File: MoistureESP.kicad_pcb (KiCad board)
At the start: 2 copper layers, 106 parts, among them J1 Conn_01x02_Pin, J2 Conn_MoisturePCB, J3 Conn_DS18B20, J4 Conn_01x06_Pin, J5 Conn_01x03_Pin, J7 USB4110-GF-A, Q1 SSM6K513NU-LF, Q10 SI7137DP-T1-GE3, Q2 SSM6K513NU-LF, Q3 2N7002W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

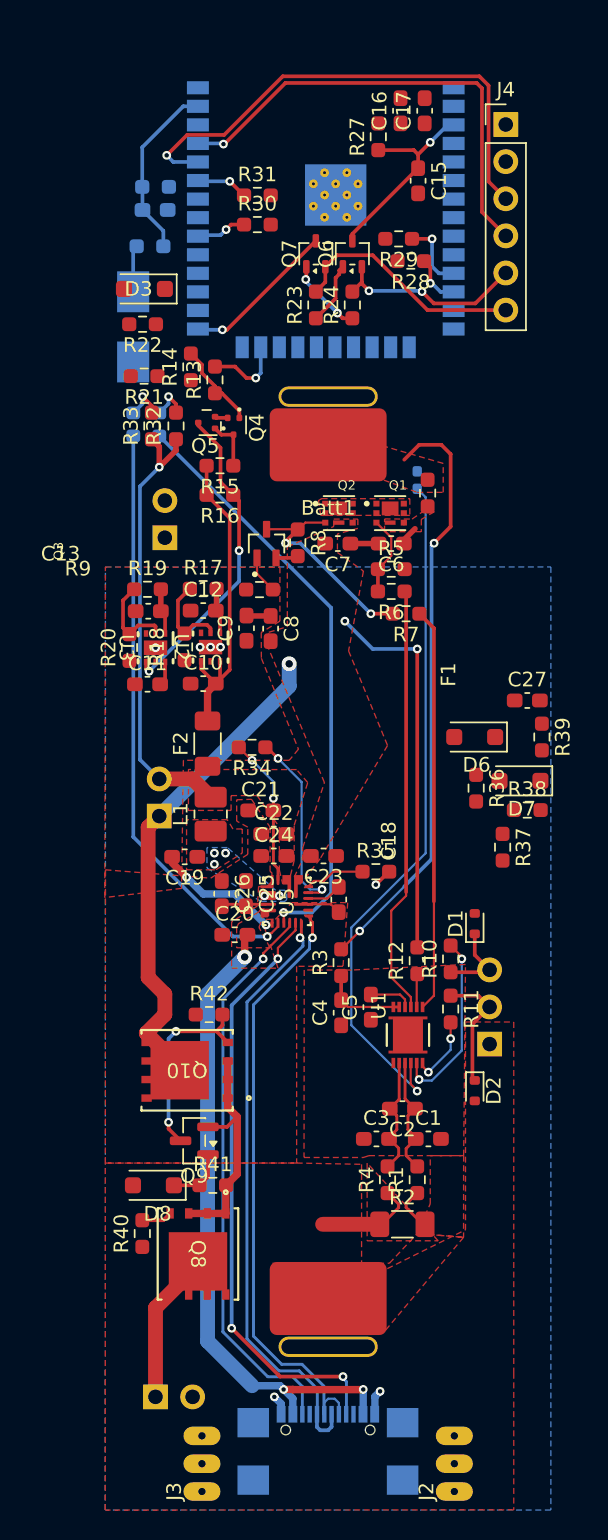
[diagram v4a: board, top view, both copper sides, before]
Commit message: Layout is finished with adding analog part, wiring the MCU ports and adding GNDD zones. Also add the nettie.
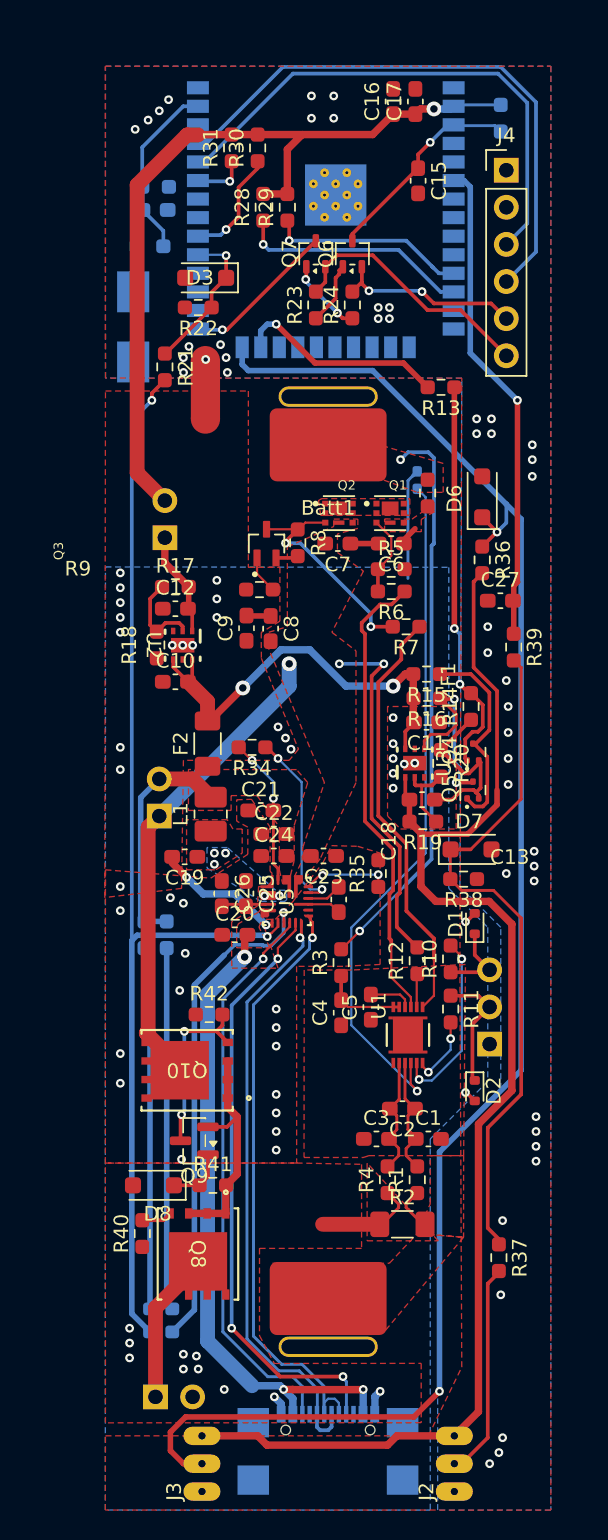
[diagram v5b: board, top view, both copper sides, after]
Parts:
- added NT1: NetTie_2, NetTie:NetTie-2_SMD_Pad2.0mm, F.Cu at (42.4, 75.7)
- R27, R32, R33: moved to B.Cu
- moved D5 61.3 mm to (38.6, 139.4)
- moved D4 61.3 mm to (40.1, 139.4)
- moved R32 34.8 mm to (39.8, 113.0), turned to -90 degrees
- moved R33 34.8 mm to (38.2, 113.0), turned to -90 degrees
- moved Q5 31.1 mm to (60.7, 103.1), turned to 90 degrees
- moved R14 30.1 mm to (60.6, 97.4)
- moved R37 28.1 mm to (62.5, 135.1)
- moved Q4 27.7 mm to (60.7, 100.5), turned to 90 degrees
- moved R19 24.6 mm to (57.3, 105.3), turned to 180 degrees
- moved C13 22.7 mm to (57.2, 103.8), turned to 180 degrees
- moved R20 22.7 mm to (58.5, 101.3), turned to -90 degrees
- moved R15 20.1 mm to (57.5, 95.2)
- moved R16 19.9 mm to (57.6, 96.8)
- moved U3 19.4 mm to (56.7, 101.3), turned to 90 degrees
- moved C11 19.3 mm to (57.5, 98.5), turned to 180 degrees
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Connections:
- D1 pad 2: GNDD -> GNDPWR
- D2 pad 2: GNDD -> GNDPWR
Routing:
- net /mcu/onewire_pin: track 0.00 -> 115.1 mm, vias 0 -> 2
- net Van: track 3.14 -> 93.6 mm
- net VDD: track 0.00 -> 55.7 mm, vias 0 -> 1
- net Net-(D7-K): track 0.00 -> 47.5 mm
- net /charger/~{INOK}: track 40.9 -> 77.5 mm, vias 1 -> 2
- net /mcu/analog_pin: track 0.00 -> 33.4 mm, vias 0 -> 1
- net Net-(D4-A): track 2.69 -> 24.8 mm, vias 1 -> 0
- net Net-(D5-A): track 2.74 -> 24.8 mm, vias 1 -> 0
- net Net-(Q4-G): track 6.06 -> 27.2 mm, vias 0 -> 2
- net GNDPWR: track 11.9 -> 31.8 mm, vias 7 -> 51
- net Vsys: track 31.0 -> 15.9 mm, vias 1 -> 0
- net /sens/moistv_sensor: track 0.00 -> 14.7 mm
- net /mcu/Disp.SCL: track 3.53 -> 16.0 mm
- net Net-(Q4-D): track 3.57 -> 14.2 mm
- net /mcu/~{CHG_INOK_PROT}: track 0.00 -> 10.4 mm, vias 0 -> 1
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- added copper zone on B.Cu, net GNDD
- added copper zone on F.Cu, net GNDD

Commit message: Fixing DRCs. Modify polygons.
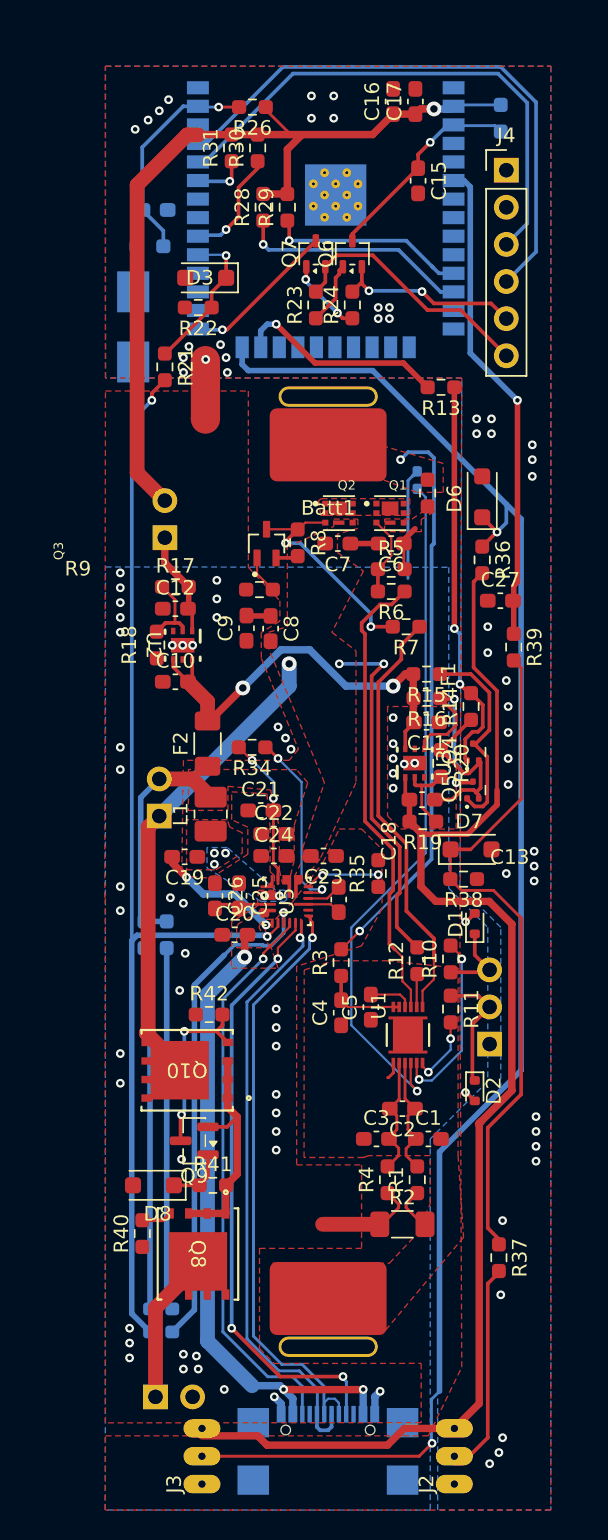
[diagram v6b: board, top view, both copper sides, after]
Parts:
- R26: moved to F.Cu
- moved R26 8.59 mm to (45.6, 56.4)
- moved J2 0.51 mm to (59.4, 150.6)
- moved J3 0.51 mm to (42.2, 150.6)
- moved C26 0.49 mm to (43.1, 110.4)
- moved C25 0.49 mm to (44.7, 110.4)
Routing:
- net /mcu/onewire_pin: track 115.1 -> 111.6 mm
- net /mcu/~{force_wakeup_prot}: track 12.3 -> 15.2 mm, vias 0 -> 1
- net VDD: track 55.7 -> 58.2 mm
- net Net-(C6-Pad1): track 1.34 -> 3.11 mm
- net CGND: track 3.08 -> 4.28 mm
- net Net-(U2-FB_NC): track 6.03 -> 5.30 mm
- net Net-(U5-BYP): track 3.04 -> 3.58 mm

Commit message: Fix the actual DRC errors, add 3D model for cell. Fix also BQ28Z610 model.
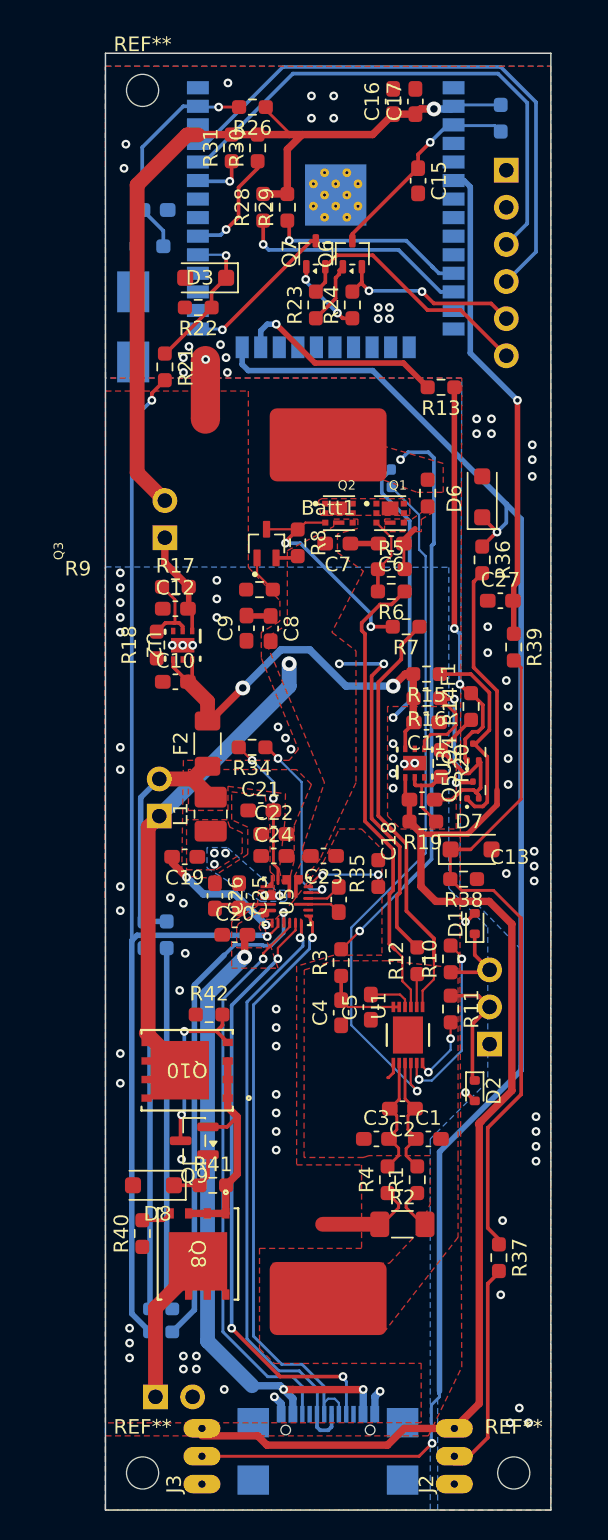
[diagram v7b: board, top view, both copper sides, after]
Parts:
- added REF**: MountingHole_2.2mm_M2, MountingHole:MountingHole_2.2mm_M2, F.Cu at (38.1, 149.9)
- added REF**: MountingHole_2.2mm_M2, MountingHole:MountingHole_2.2mm_M2, F.Cu at (38.1, 55.2)
- added REF**: MountingHole_2.2mm_M2, MountingHole:MountingHole_2.2mm_M2, F.Cu at (63.5, 149.9)
- J4: moved to B.Cu
- moved TH1 1.78 mm to (55.1, 81.8)
- turned J4 to 180 degrees
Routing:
- net GNDPWR: track 31.8 -> 43.9 mm
- net Vsys: track 15.9 -> 17.3 mm
- net Net-(U1-TS1): track 47.5 -> 48.4 mm
- net GNDD: vias 46 -> 45
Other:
- board outline added: 30.5 x 99.7 mm

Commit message: Fix ESP32 GPIO wiring, many bootstrap pins were used.
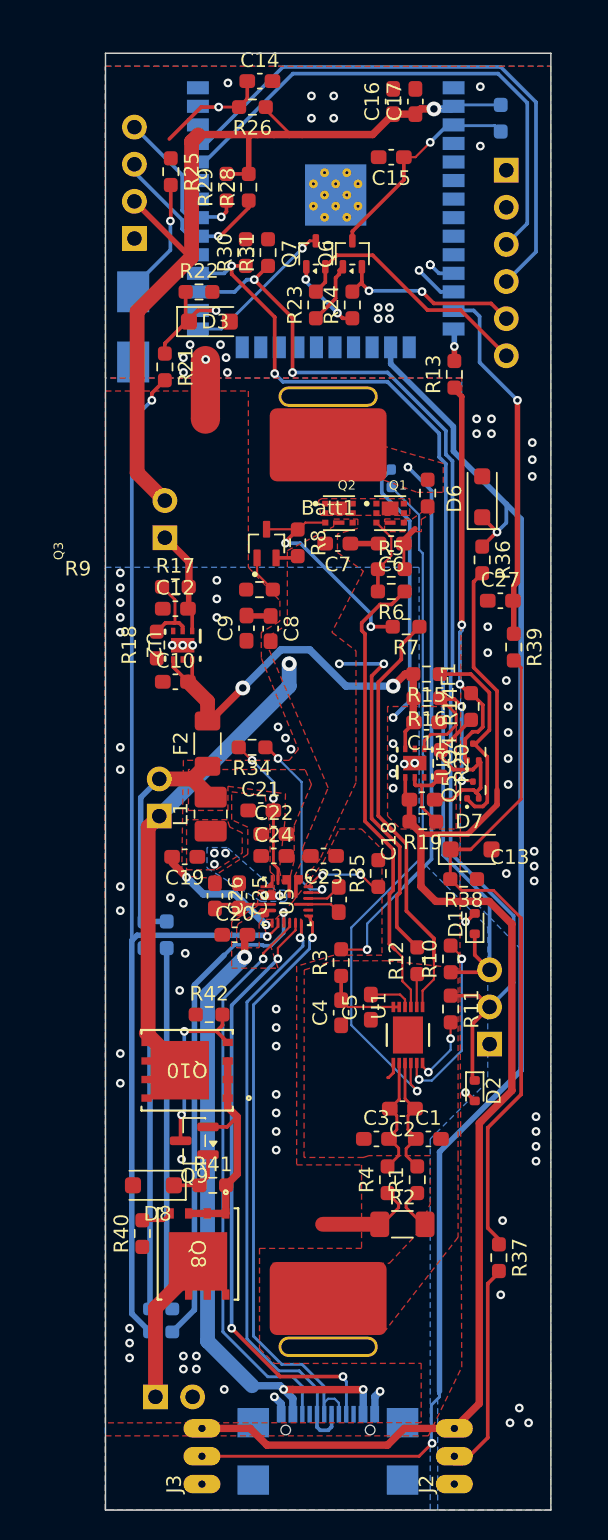
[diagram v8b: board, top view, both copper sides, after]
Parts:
- removed REF** (x3): MountingHole_2.2mm_M2, MountingHole:MountingHole_2.2mm_M2
- added J6: Conn_01x04_Pin, Connector_PinHeader_2.54mm:PinHeader_1x04_P2.54mm_Vertical, B.Cu at (37.5, 65.4)
- C14, R25: moved to F.Cu
- moved C14 11.4 mm to (46.1, 54.6)
- moved R31 7.58 mm to (46.7, 66.3)
- moved R30 7.21 mm to (45.2, 66.3)
- moved R25 5.30 mm to (40.0, 60.8), turned to -90 degrees
- moved R29 4.39 mm to (43.8, 61.9)
- moved D3 3.01 mm to (42.7, 71.1), turned to 0 degrees
- moved C15 2.45 mm to (55.1, 59.8), turned to 180 degrees
- moved R28 1.69 mm to (45.4, 61.9)
- moved R13 1.27 mm to (59.4, 74.7), turned to 90 degrees
- moved R22 1.07 mm to (42.0, 69.0), turned to 0 degrees
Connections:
- R30 pad 1: /mcu/BATT_I2C.SCL -> /battery/comm.SCL
- R31 pad 1: /mcu/BATT_I2C.SDA -> /battery/comm.SDA
- U4 pad 10: unconnected-(U4-IO25-Pad10) -> /mcu/analog_enable
- U4 pad 11: /mcu/Disp.SDA -> unconnected-(U4-IO26-Pad11)
- U4 pad 12: /mcu/Disp.SCL -> /mcu/onewire_pin
- U4 pad 23: /mcu/analog_enable -> unconnected-(U4-IO15-Pad23)
- U4 pad 24: /mcu/onewire_pin -> unconnected-(U4-IO2-Pad24)
- U4 pad 26: unconnected-(U4-IO4-Pad26) -> /mcu/~{CHG_INOK_PROT}
- U4 pad 27: unconnected-(U4-IO16-Pad27) -> /battery/comm.SDA
- U4 pad 28: unconnected-(U4-IO17-Pad28) -> /battery/comm.SCL
- U4 pad 29: /mcu/~{CHG_INOK_PROT} -> unconnected-(U4-IO5-Pad29)
- U4 pad 30: /mcu/BATT_I2C.SCL -> /mcu/Disp.SCL
- U4 pad 31: unconnected-(U4-IO19-Pad31) -> /mcu/Disp.SDA
- U4 pad 33: /mcu/BATT_I2C.SDA -> unconnected-(U4-IO21-Pad33)
- U4 pad 6: /mcu/analog_pin -> unconnected-(U4-IO34-Pad6)
- U4 pad 7: unconnected-(U4-IO35-Pad7) -> /mcu/analog_pin
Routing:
- net /battery/comm.SDA: track 8.73 -> 76.0 mm, vias 0 -> 2
- net /battery/comm.SCL: track 5.62 -> 68.9 mm, vias 0 -> 2
- net /mcu/analog_enable: track 14.5 -> 2.21 mm
- net /mcu/analog_pin: track 33.4 -> 24.9 mm
- net /mcu/BATT_I2C.SCL: track 7.69 -> 0.00 mm, vias 1 -> 0
- net /mcu/onewire_pin: track 111.6 -> 105.4 mm, vias 2 -> 3
- net /mcu/~{force_wakeup_prot}: track 15.2 -> 9.13 mm
- net /mcu/~{force_wakeup}: track 3.22 -> 8.38 mm, vias 0 -> 1
- net /mcu/Disp.SCL: track 16.0 -> 11.8 mm
- net /mcu/BATT_I2C.SDA: track 3.63 -> 0.00 mm, vias 1 -> 0
- net VDD: track 58.2 -> 61.6 mm
- net /mcu/Disp.SDA: track 13.7 -> 11.2 mm
- net /mcu/~{CHG_INOK_PROT}: track 10.4 -> 8.55 mm
- net unconnected-(U4-IO26-Pad11): track 0.00 -> 1.86 mm, vias 0 -> 2
- net /battery/Vcell+: track 39.0 -> 37.3 mm
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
